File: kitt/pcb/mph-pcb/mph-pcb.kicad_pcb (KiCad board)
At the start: 4 copper layers, 280 x 125 mm, 136 parts, among them J1 Screw_Terminal_01x02, J2 Screw_Terminal_01x03, U1 TLC5940NT, U2 TLC5940NT, U3 TLC5940NT, U4 TLC5940NT, U5 TLC5940NT, U6 TLC5940NT, U7 TLC5940NT

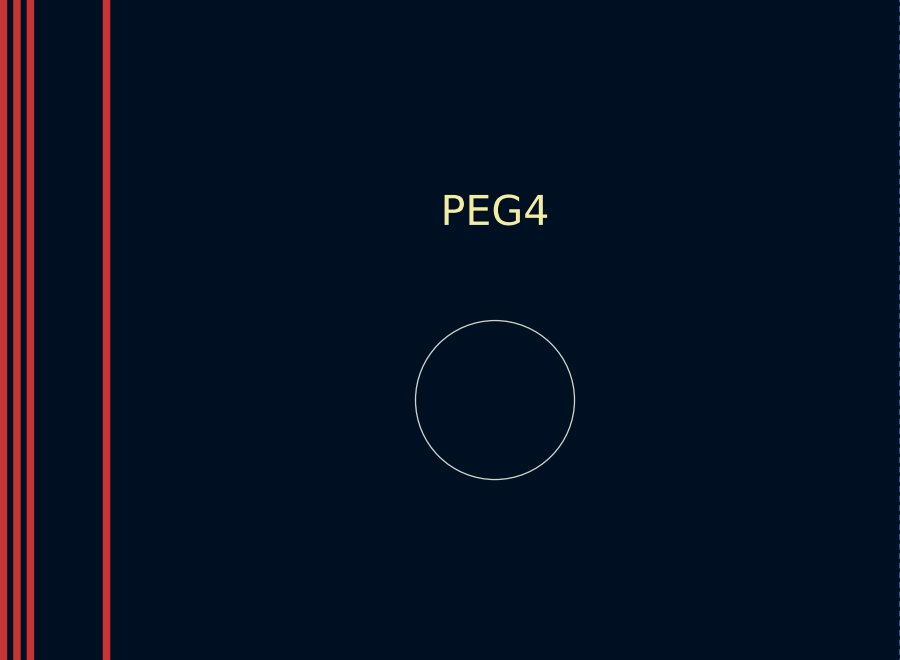
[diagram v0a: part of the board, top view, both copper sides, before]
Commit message: fixed pegboard spacing
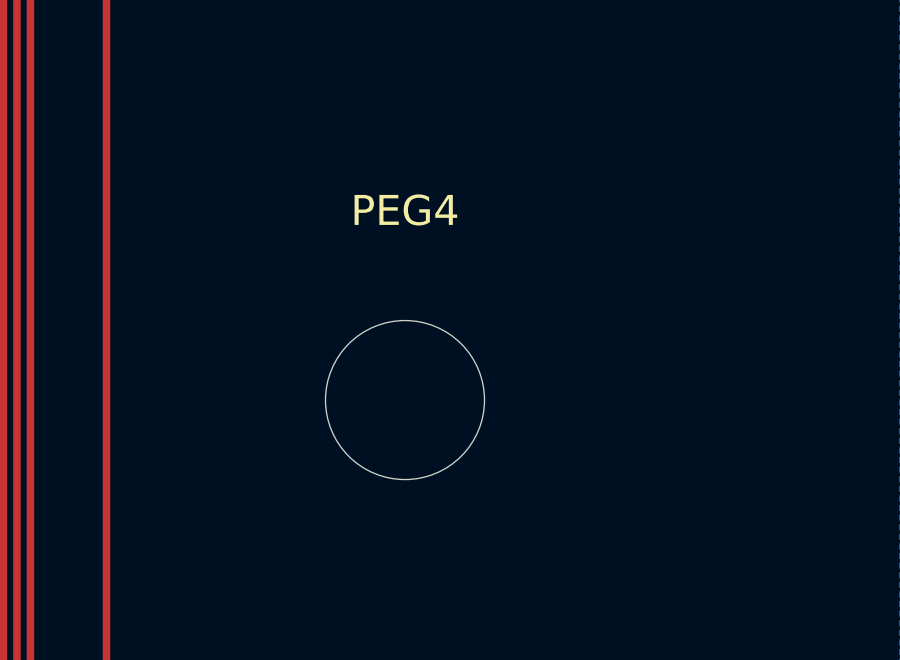
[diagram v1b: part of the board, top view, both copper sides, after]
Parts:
- moved PEG4 3.00 mm to (283.0, 128.0)

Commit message: changed for new optoelectronics
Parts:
- removed the R12 at (96.4, 63.8)
- removed the R13 at (93.3, 63.8)
- removed the R21 at (221.5, 66.3)
- removed the R23 at (227.9, 66.3)
- removed R29, R31: 120R, Resistor_THT:R_Axial_DIN0207_L6.3mm_D2.5mm_P10.16mm_Horizontal
- removed the R8 at (80.6, 63.8)
- added Q1: NDP6020P, Package_TO_SOT_THT:TO-220-3_Horizontal_TabDown, F.Cu at (40.6, 84.7)
- added Q2: NDP6020P, Package_TO_SOT_THT:TO-220-3_Horizontal_TabDown, F.Cu at (145.0, 67.3)
- added R24: 220R, Resistor_THT:R_Axial_DIN0207_L6.3mm_D2.5mm_P10.16mm_Horizontal, F.Cu at (52.5, 77.3)
- added R26: 220R, Resistor_THT:R_Axial_DIN0207_L6.3mm_D2.5mm_P10.16mm_Horizontal, F.Cu at (171.5, 52.3)
- J2: value Screw_Terminal_01x03 -> Screw_Terminal_01x02; footprint KITT-Footpads:5mm_Screw_Terminal_01x03 -> KITT-Footpads:5mm_Screw_Terminal_01x02
- R10, R11, R25, R27, R9: value 120R -> 22R
- R12: renamed from R14; value 120R -> 22R
- R13: renamed from R15; value 120R -> 22R
- R14: renamed from R16; value 120R -> 22R
- R15: renamed from R17; value 120R -> 22R
- R16: renamed from R18; value 120R -> 22R
- R17: renamed from R19; value 120R -> 22R
- R18: renamed from R20; value 120R -> 22R
- R19: renamed from R22; value 120R -> 22R
- R20: renamed from R24; value 120R -> 22R
- R21: renamed from R26; value 120R -> 22R
- R22: renamed from R28; value 120R -> 22R
- R23: renamed from R30; value 120R -> 22R
- moved R25 185.4 mm to (49.5, 81.3), turned to 0 degrees
- moved R10 79.0 mm to (145.3, 98.1), turned to 180 degrees
- moved R9 74.5 mm to (145.3, 94.2), turned to 180 degrees
- moved R11 59.5 mm to (145.3, 101.9), turned to 180 degrees
- moved R27 55.9 mm to (186.5, 52.3), turned to 0 degrees
- moved THRU1 8.84 mm to (108.0, 152.4)
- moved R14 8.41 mm to (98.5, 63.8)
- moved R13 8.08 mm to (95.0, 63.8)
- moved R12 7.76 mm to (91.5, 63.8)
- moved R23 4.45 mm to (245.7, 66.3)
- moved R22 3.17 mm to (240.6, 66.3)
- moved HY1 2.54 mm to (117.4, 70.1), turned to 180 degrees
- moved HY2 2.54 mm to (122.5, 70.1), turned to 180 degrees
- moved HY3 2.54 mm to (127.6, 70.1), turned to 180 degrees
- moved MSGY1 2.54 mm to (155.5, 101.9), turned to 180 degrees
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- renumbered R32 to R1, R1 to R2, R2 to R3, R3 to R4, R4 to R5, R5 to R6, R6 to R7, R7 to R8
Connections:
- net /LV_MSG_TX renamed /UG_YD
- GUID1 pad 2: GND -> Net-(GUID1-Pad2)
- GUID1 pad 4: GND -> Net-(GUID1-Pad4)
- GUID1 pad 6: GND -> Net-(GUID1-Pad6)
- GUID2 pad 2: GND -> Net-(GUID2-Pad2)
- GUID2 pad 4: GND -> Net-(GUID2-Pad4)
- GUID2 pad 6: GND -> Net-(GUID2-Pad6)
- HY1 pad 1: /HLT_YD1 -> Net-(HY1-Pad1)
- HY2 pad 1: /HLT_YD2 -> Net-(HY2-Pad1)
- HY3 pad 1: /HLT_YD3 -> Net-(HY3-Pad1)
- LVL1 pad 5: /HV_MSG_TX -> /UG_YD_MOSFET
- LVL1 pad 6: Net-(LVL1-Pad6) -> /MASH_YD_MOSFET
- LVL1 pad 7: Net-(LVL1-Pad7) -> /MASH_YD
- MASH_DISP1 pad 6: Net-(MASH_DISP1-Pad6) -> (no net)
- MASH_DISP2 pad 6: Net-(MASH_DISP2-Pad6) -> (no net)
- MASH_DISP3 pad 6: Net-(MASH_DISP3-Pad6) -> (no net)
- MASH_DISP4 pad 6: Net-(MASH_DISP4-Pad6) -> (no net)
- MPH1 pad 1: GND -> Net-(MPH1-Pad1)
- MPH1 pad 3: Net-(MPH1-Pad3) -> Net-(MPH1-Pad1)
- MPH1 pad 5: GND -> Net-(MPH1-Pad5)
- MPH1 pad 7: Net-(MPH1-Pad7) -> Net-(MPH1-Pad5)
- MPH2 pad 1: GND -> Net-(MPH2-Pad1)
- MPH2 pad 3: Net-(MPH2-Pad3) -> Net-(MPH2-Pad1)
- MPH2 pad 5: GND -> Net-(MPH2-Pad5)
- MPH2 pad 7: Net-(MPH2-Pad7) -> Net-(MPH2-Pad5)
- MPH3 pad 1: GND -> Net-(MPH3-Pad1)
- MPH3 pad 3: Net-(MPH3-Pad3) -> Net-(MPH3-Pad1)
- MPH3 pad 5: GND -> Net-(MPH3-Pad5)
- MPH3 pad 7: Net-(MPH3-Pad7) -> Net-(MPH3-Pad5)
- MSGY1 pad 1: /UT_YD1 -> Net-(MSGY1-Pad1)
- MSGY1 pad 2: +5V -> Net-(HY1-Pad1)
- MSGY2 pad 1: /UT_YD2 -> Net-(MSGY2-Pad1)
- MSGY2 pad 2: +5V -> Net-(HY2-Pad1)
- MSGY3 pad 1: /UT_YD3 -> Net-(MSGY3-Pad1)
- MSGY3 pad 2: +5V -> Net-(HY3-Pad1)
- MY1 pad 1: /MASH_YD1 -> Net-(MY1-Pad1)
- MY1 pad 2: +5V -> Net-(MY1-Pad2)
- MY2 pad 1: /MASH_YD2 -> Net-(MY2-Pad1)
- MY2 pad 2: +5V -> Net-(MY1-Pad2)
- MY3 pad 1: /MASH_YD3 -> Net-(MY3-Pad1)
- MY3 pad 2: +5V -> Net-(MY2-Pad1)
- R10 pad 1: +5V -> Net-(MSGY2-Pad1)
- R10 pad 2: Net-(R10-Pad2) -> GND
- R11 pad 1: +5V -> Net-(MSGY3-Pad1)
- R11 pad 2: Net-(R11-Pad2) -> GND
- R25 pad 1: +5V -> Net-(MY3-Pad1)
- R25 pad 2: Net-(MPH2-Pad3) -> GND
- R27 pad 1: +5V -> Net-(R27-Pad1)
- R27 pad 2: Net-(MPH2-Pad7) -> GND
- R9 pad 1: +5V -> Net-(MSGY1-Pad1)
- R9 pad 2: Net-(R9-Pad2) -> GND
- SYST1 pad 1: Net-(R10-Pad2) -> Net-(GUID1-Pad2)
- SYST1 pad 3: Net-(R9-Pad2) -> Net-(GUID1-Pad4)
- SYST1 pad 5: Net-(R8-Pad2) -> Net-(GUID1-Pad6)
- SYST2 pad 1: Net-(R13-Pad2) -> Net-(GUID2-Pad2)
- SYST2 pad 3: Net-(R12-Pad2) -> Net-(GUID2-Pad4)
- SYST2 pad 5: Net-(R11-Pad2) -> Net-(GUID2-Pad6)
- TTGO1 pad 11: Net-(TTGO1-Pad11) -> (no net)
- TTGO1 pad 12: Net-(TTGO1-Pad12) -> (no net)
- TTGO1 pad 18: Net-(TTGO1-Pad18) -> /MASH_YD
- TTGO1 pad 19: Net-(TTGO1-Pad19) -> (no net)
- TTGO1 pad 8: Net-(TTGO1-Pad8) -> (no net)
- U1 pad 16: Net-(U1-Pad16) -> (no net)
- U2 pad 16: Net-(U2-Pad16) -> (no net)
- U3 pad 16: Net-(U3-Pad16) -> (no net)
- U4 pad 1: /MASH_YD2 -> (no net)
- U4 pad 10: /UT_YD2 -> /UG_D1
- U4 pad 11: /UT_YD3 -> /UG_D2
- U4 pad 12: /UG_D1 -> /UG_D3
- U4 pad 13: /UG_D2 -> /UG_D4
- U4 pad 14: /UG_D3 -> /UG_D5
- U4 pad 15: /UG_D4 -> (no net)
- U4 pad 16: Net-(U4-Pad16) -> (no net)
- U4 pad 2: /MASH_YD3 -> (no net)
- U4 pad 28: /MASH_YD1 -> (no net)
- U4 pad 3: /HLT_YD1 -> (no net)
- U4 pad 4: /HLT_YD2 -> (no net)
- U4 pad 5: /HLT_YD3 -> (no net)
- U4 pad 6: /UG_YD1 -> (no net)
- U4 pad 7: /UG_YD2 -> (no net)
- U4 pad 8: /UG_YD3 -> (no net)
- U4 pad 9: /UT_YD1 -> (no net)
- U5 pad 16: Net-(U5-Pad16) -> (no net)
- U5 pad 28: /UG_D5 -> (no net)
- U6 pad 16: Net-(U6-Pad16) -> (no net)
- U7 pad 10: Net-(U7-Pad10) -> (no net)
- U7 pad 11: Net-(U7-Pad11) -> (no net)
- U7 pad 12: Net-(U7-Pad12) -> (no net)
- U7 pad 13: Net-(U7-Pad13) -> (no net)
- U7 pad 14: Net-(U7-Pad14) -> (no net)
- U7 pad 15: Net-(U7-Pad15) -> (no net)
- U7 pad 16: Net-(U7-Pad16) -> (no net)
- U7 pad 8: Net-(U7-Pad8) -> (no net)
- U7 pad 9: Net-(U7-Pad9) -> (no net)
- UGY1 pad 1: /UG_YD1 -> Net-(R26-Pad1)
- UGY1 pad 2: +5V -> Net-(Q2-Pad2)
- UGY2 pad 1: /UG_YD2 -> Net-(UGY2-Pad1)
- UGY2 pad 2: +5V -> Net-(Q2-Pad2)
- UGY3 pad 1: /UG_YD3 -> Net-(R27-Pad1)
- UGY3 pad 2: +5V -> Net-(UGY2-Pad1)
- UT_DISP1 pad 6: Net-(UT_DISP1-Pad6) -> (no net)
- UT_DISP2 pad 6: Net-(UT_DISP2-Pad6) -> (no net)
- UT_DISP3 pad 6: Net-(UT_DISP3-Pad6) -> (no net)
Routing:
- net /MASH_YD_MOSFET: track 0.00 -> 279.4 mm
- net /UG_YD_MOSFET: track 0.00 -> 213.5 mm
- net /MASH_YD: track 0.00 -> 136.0 mm
- net /MASH_YD1: track 102.7 -> 0.00 mm
- net /MASH_YD3: track 102.6 -> 0.00 mm
- net /MASH_YD2: track 97.5 -> 0.00 mm
- net /DCPRG: track 670.3 -> 605.6 mm
- net Net-(HY3-Pad1): track 0.00 -> 54.7 mm
- net Net-(HY2-Pad1): track 0.00 -> 53.2 mm
- net Net-(HY1-Pad1): track 0.00 -> 52.0 mm
- net /UT_YD3: track 48.7 -> 0.00 mm
- net /UT_YD2: track 47.7 -> 0.00 mm
- net /UT_YD1: track 46.6 -> 0.00 mm
- net /UG_YD3: track 35.2 -> 0.00 mm
- net /UG_YD2: track 32.6 -> 0.00 mm
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
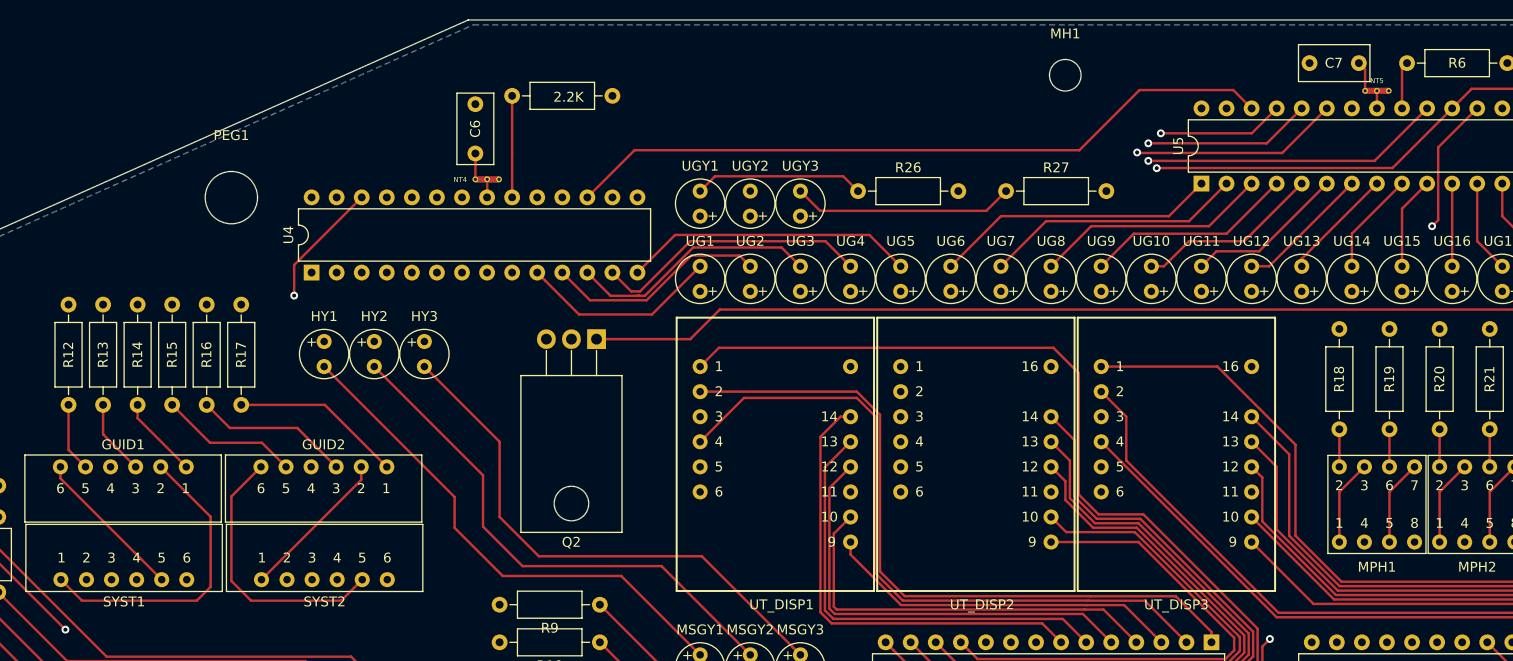
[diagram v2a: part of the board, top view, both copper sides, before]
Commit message: get rid of some vias
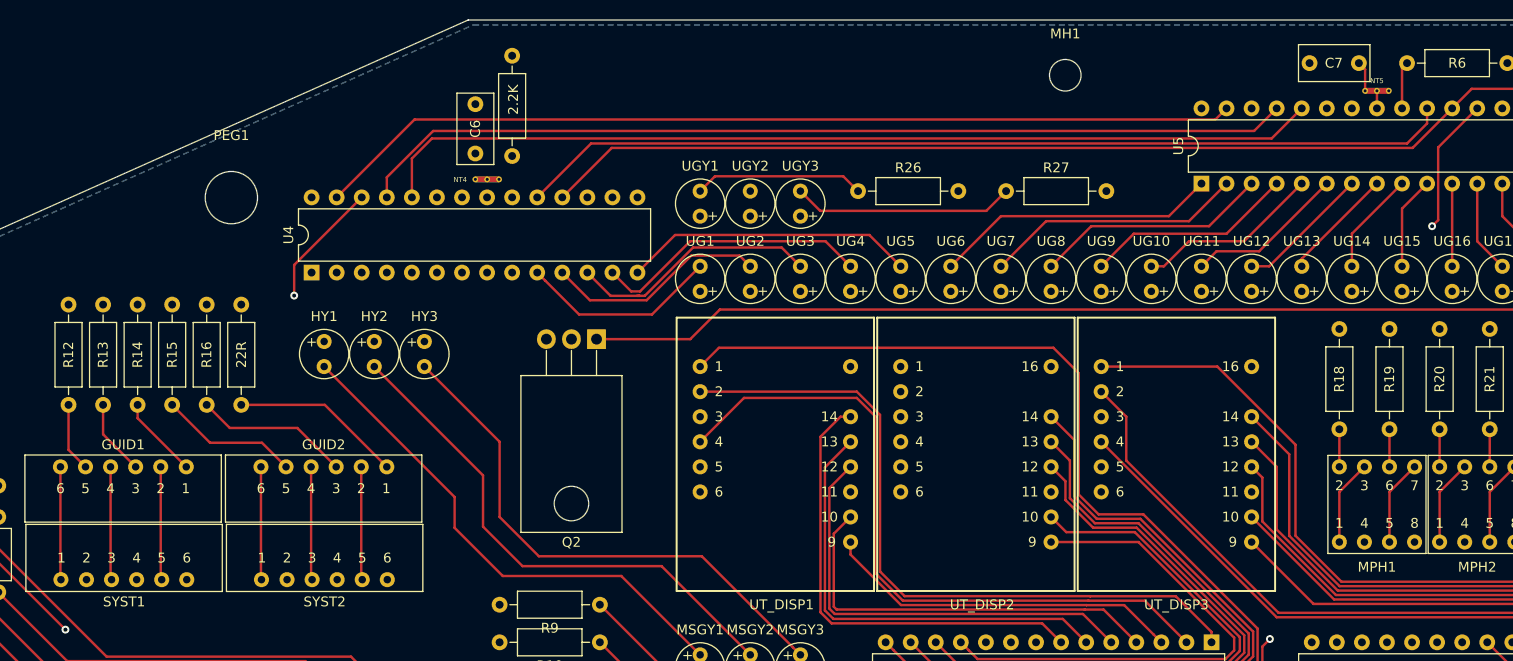
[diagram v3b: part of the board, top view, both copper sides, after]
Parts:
- moved R5 6.10 mm to (136.4, 48.8), turned to 90 degrees
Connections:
- SYST1 pad 1: Net-(GUID1-Pad2) -> Net-(GUID1-Pad6)
- SYST1 pad 5: Net-(GUID1-Pad6) -> Net-(GUID1-Pad2)
- SYST2 pad 1: Net-(GUID2-Pad2) -> Net-(GUID2-Pad6)
- SYST2 pad 5: Net-(GUID2-Pad6) -> Net-(GUID2-Pad2)
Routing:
- net Net-(GUID1-Pad2): track 30.9 -> 11.5 mm
- net Net-(GUID2-Pad6): track 27.8 -> 11.5 mm
- net Net-(R5-Pad1): track 10.3 -> 4.19 mm
- net Net-(GUID1-Pad6): track 15.7 -> 11.5 mm
- net Net-(GUID2-Pad2): track 15.6 -> 11.5 mm
- net /BLANK: track 606.4 -> 608.2 mm, vias 2 -> 1
- net /DCPRG: track 605.6 -> 606.8 mm, vias 2 -> 1
- net Net-(C6-Pad1): track 2.00 -> 2.62 mm
- net /XLAT: track 617.4 -> 617.8 mm, vias 2 -> 1
- net /SCLK: track 621.4 -> 621.8 mm, vias 1 -> 0
- net /GSCLK: track 594.7 -> 594.9 mm, vias 2 -> 1

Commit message: label components
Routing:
- net /SIG_1: track 344.9 -> 347.3 mm

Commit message: fixed footprints for mph leds
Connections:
- MPH1 pad 1: Net-(MPH1-Pad1) -> GND
- MPH1 pad 3: Net-(MPH1-Pad1) -> Net-(MPH1-Pad3)
- MPH1 pad 5: Net-(MPH1-Pad5) -> Net-(MPH1-Pad3)
- MPH1 pad 7: Net-(MPH1-Pad5) -> Net-(MPH1-Pad7)
- MPH1 pad 8: GND -> Net-(MPH1-Pad2)
- MPH2 pad 1: Net-(MPH2-Pad1) -> GND
- MPH2 pad 3: Net-(MPH2-Pad1) -> Net-(MPH2-Pad3)
- MPH2 pad 5: Net-(MPH2-Pad5) -> Net-(MPH2-Pad3)
- MPH2 pad 7: Net-(MPH2-Pad5) -> Net-(MPH2-Pad7)
- MPH2 pad 8: GND -> Net-(MPH2-Pad2)
- MPH3 pad 1: Net-(MPH3-Pad1) -> GND
- MPH3 pad 3: Net-(MPH3-Pad1) -> Net-(MPH3-Pad3)
- MPH3 pad 5: Net-(MPH3-Pad5) -> Net-(MPH3-Pad3)
- MPH3 pad 7: Net-(MPH3-Pad5) -> Net-(MPH3-Pad7)
- MPH3 pad 8: GND -> Net-(MPH3-Pad2)
- R18 pad 2: Net-(MPH1-Pad2) -> Net-(MPH1-Pad7)
- R20 pad 2: Net-(MPH2-Pad2) -> Net-(MPH2-Pad7)
- R21 pad 1: +5V -> (no net)
- R22 pad 2: Net-(MPH3-Pad2) -> Net-(MPH3-Pad7)
- R23 pad 1: +5V -> (no net)
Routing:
- net Net-(MPH3-Pad5): track 8.67 -> 0.00 mm
- net Net-(MPH2-Pad5): track 8.67 -> 0.00 mm
- net Net-(MPH3-Pad3): track 0.00 -> 8.67 mm
- net Net-(MPH2-Pad3): track 0.00 -> 8.67 mm
- net Net-(MPH3-Pad1): track 8.67 -> 0.00 mm
- net Net-(MPH2-Pad1): track 8.67 -> 0.00 mm
- net Net-(MPH1-Pad5): track 8.67 -> 0.00 mm
- net Net-(MPH1-Pad1): track 8.67 -> 0.00 mm
- net Net-(MPH1-Pad3): track 0.00 -> 8.67 mm
- net Net-(MPH3-Pad7): track 0.00 -> 4.86 mm
- net Net-(MPH3-Pad2): track 3.81 -> 8.67 mm
- net Net-(MPH2-Pad7): track 0.00 -> 4.86 mm
- net Net-(MPH2-Pad2): track 3.81 -> 8.67 mm
- net Net-(MPH1-Pad7): track 0.00 -> 4.86 mm
- net Net-(MPH1-Pad2): track 3.81 -> 8.67 mm
